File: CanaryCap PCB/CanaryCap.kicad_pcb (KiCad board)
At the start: 2 copper layers, 120 x 30 mm, 59 parts, among them J1 USB_C_Receptacle_USB2.0_16P, J2 Impact Connector, J3 Gas Connector, J4 Battery Connector, Q1 NMOS, Q2 PMOS_Substrate, SW1 SW_MEC_5E, SW2 SW_MEC_5E, SW3 SW_MEC_5E, U1 LMZM23601V5, U2 LM3940 3.3V-SOT223, U3 ESP32-C6FH4, U4 ADXL343

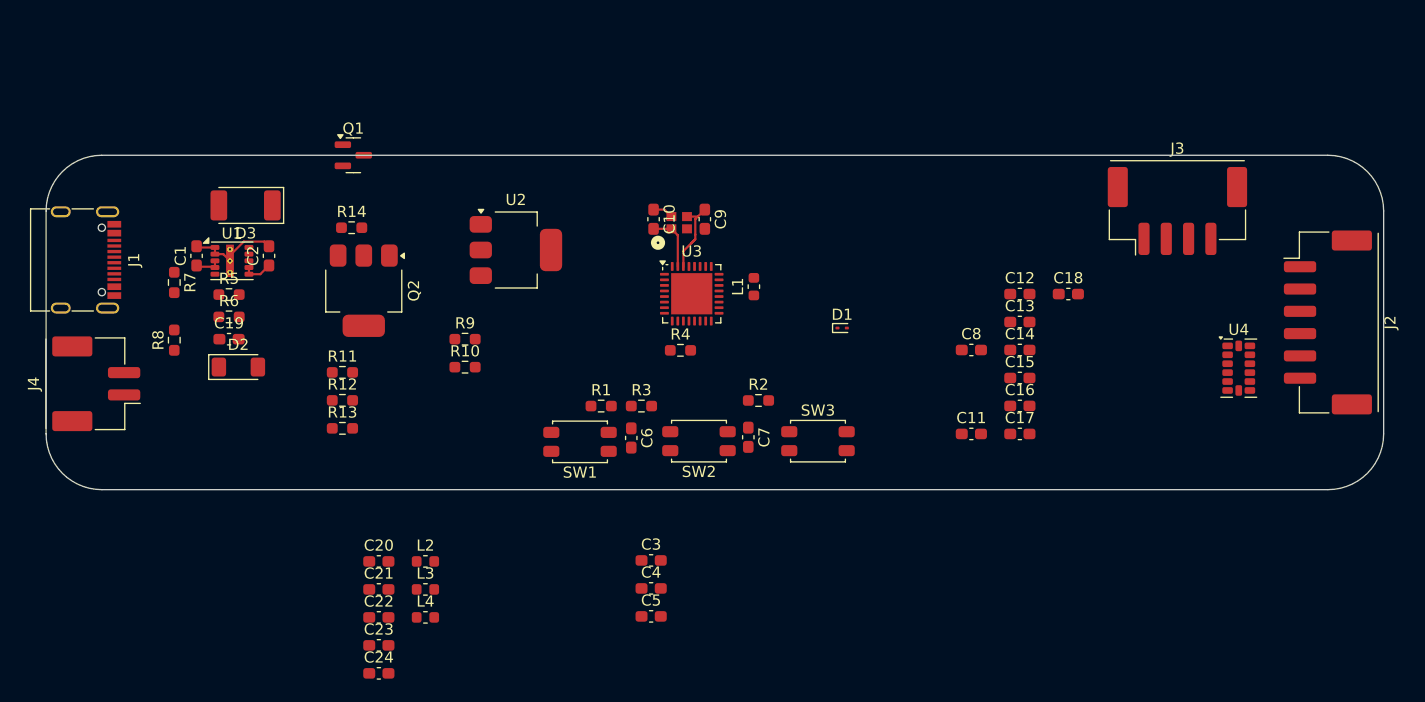
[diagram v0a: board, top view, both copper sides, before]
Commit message: Deleted windows blink
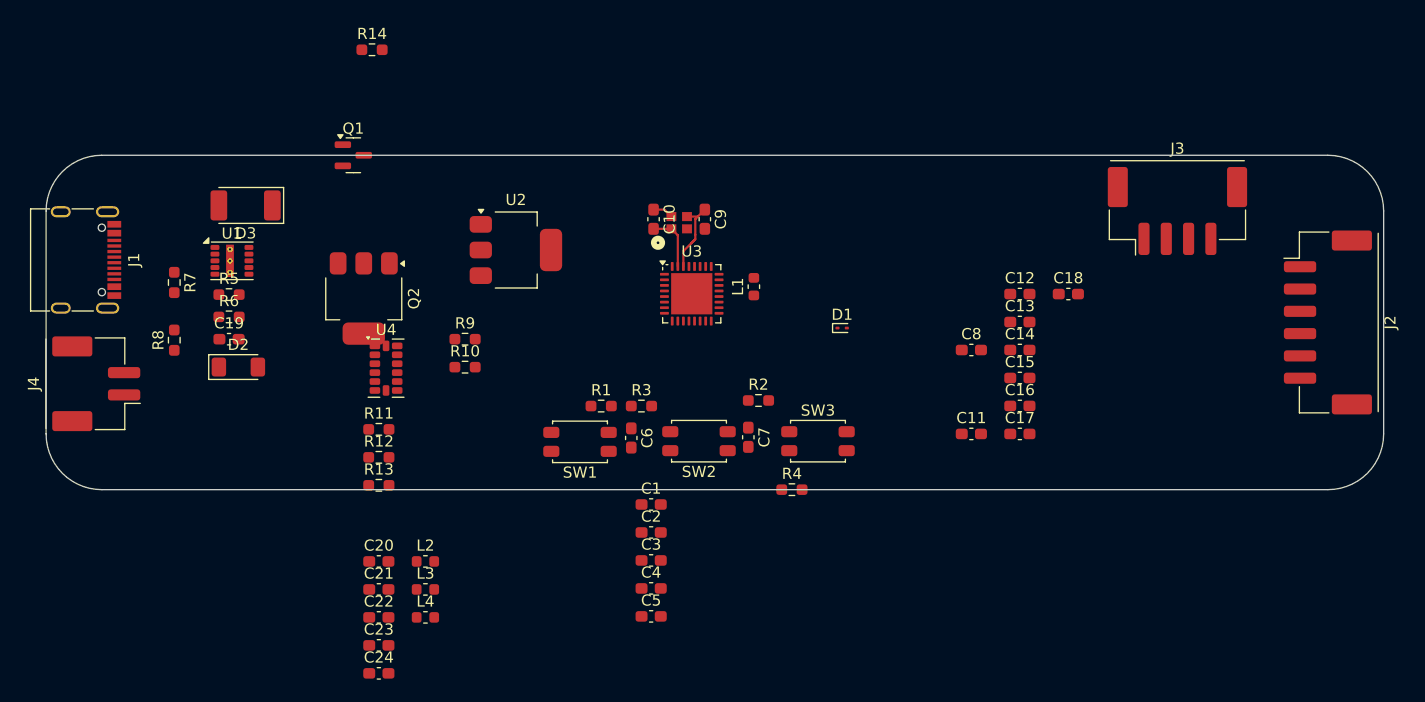
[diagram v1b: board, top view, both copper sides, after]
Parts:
- moved U4 76.5 mm to (131.0, -10.9)
- moved C1 46.5 mm to (154.8, 1.33), turned to 0 degrees
- moved C2 42.3 mm to (154.8, 3.84), turned to 0 degrees
- moved R14 16.1 mm to (129.7, -39.5)
- moved R4 16.0 mm to (167.4, 0.00)
- moved R11 6.06 mm to (130.4, -5.41)
- moved R12 6.06 mm to (130.4, -2.90)
- moved R13 6.06 mm to (130.4, -0.39)
- moved Q2 0.70 mm to (129.0, -17.1)
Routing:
- net GNDREF: track 10.4 -> 1.86 mm
- net +5V_buck: track 2.72 -> 0.00 mm
- net +12V: track 2.28 -> 0.00 mm
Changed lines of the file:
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@@
 	(footprint "Resistor_SMD:R_0603_1608Metric_Pad0.98x0.95mm_HandSolder"
 		(layer "F.Cu")
-		(at 127.0875 -5.5)
+		(at 130.353301 -0.389701)
 		(descr "Resistor SMD 0603 (1608 Metric), square (rectangular) end terminal, IPC-7351 nominal with elongated pad for handsoldering. (Body size source: IPC-SM-782 page 72, https://www.pcb-3d.com/wordpress/wp-content/uploads/ipc-sm-782a_amendment_1_and_2.pdf), generated with kicad-footprint-generator")
 		(tags "resistor handsolder")
@@
 	(footprint "Resistor_SMD:R_0603_1608Metric_Pad0.98x0.95mm_HandSolder"
 		(layer "F.Cu")
-		(at 127.0875 -8.01)
+		(at 130.353301 -2.899701)
 		(descr "Resistor SMD 0603 (1608 Metric), square (rectangular) end terminal, IPC-7351 nominal with elongated pad for handsoldering. (Body size source: IPC-SM-782 page 72, https://www.pcb-3d.com/wordpress/wp-content/uploads/ipc-sm-782a_amendment_1_and_2.pdf), generated with kicad-footprint-generator")
 		(tags "resistor handsolder")
@@
 	(footprint "Resistor_SMD:R_0603_1608Metric_Pad0.98x0.95mm_HandSolder"
 		(layer "F.Cu")
-		(at 127.0875 -10.52)
+		(at 130.353301 -5.409701)
 		(descr "Resistor SMD 0603 (1608 Metric), square (rectangular) end terminal, IPC-7351 nominal with elongated pad for handsoldering. (Body size source: IPC-SM-782 page 72, https://www.pcb-3d.com/wordpress/wp-content/uploads/ipc-sm-782a_amendment_1_and_2.pdf), generated with kicad-footprint-generator")
 		(tags "resistor handsolder")
@@
 	(footprint "Capacitor_SMD:C_0603_1608Metric_Pad1.08x0.95mm_HandSolder"
 		(layer "F.Cu")
-		(at 120.5 -20.975 90)
+		(at 154.783301 3.840299)
 		(descr "Capacitor SMD 0603 (1608 Metric), square (rectangular) end terminal, IPC-7351 nominal with elongated pad for handsoldering. (Body size source: IPC-SM-782 page 76, https://www.pcb-3d.com/wordpress/wp-content/uploads/ipc-sm-782a_amendment_1_and_2.pdf), generated with kicad-footprint-generator")
 		(tags "capacitor handsolder")
 		(property "Reference" "C2"
-			(at 0 -1.43 90)
+			(at 0 -1.43 0)
 			(layer "F.SilkS")
 			(effects
@@
 		)
 		(property "Value" "10uF"
-			(at 0 1.43 90)
+			(at 0 1.43 0)
 			(layer "F.Fab")
 			(effects
@@
 		)
 		(property "Datasheet" "~"
-			(at 0 0 90)
+			(at 0 0 0)
 			(layer "F.Fab")
 			(hide yes)
@@
 		)
 		(property "Description" "Unpolarized capacitor"
-			(at 0 0 90)
+			(at 0 0 0)
 			(layer "F.Fab")
 			(hide yes)
@@
 		)
 		(fp_line
-			(start 1.65 -0.73)
-			(end 1.65 0.73)
+			(start -1.65 -0.73)
+			(end 1.65 -0.73)
 			(stroke
 				(width 0.05)
@@
 		)
 		(fp_line
-			(start -1.65 -0.73)
-			(end 1.65 -0.73)
+			(start -1.65 0.73)
+			(end -1.65 -0.73)
 			(stroke
 				(width 0.05)
@@
 		)
 		(fp_line
-			(start 1.65 0.73)
-			(end -1.65 0.73)
+			(start 1.65 -0.73)
+			(end 1.65 0.73)
 			(stroke
 				(width 0.05)
@@
 		)
 		(fp_line
-			(start -1.65 0.73)
-			(end -1.65 -0.73)
+			(start 1.65 0.73)
+			(end -1.65 0.73)
 			(stroke
 				(width 0.05)
@@
 		)
 		(fp_line
-			(start 0.8 -0.4)
-			(end 0.8 0.4)
+			(start -0.8 -0.4)
+			(end 0.8 -0.4)
 			(stroke
 				(width 0.1)
@@
 		)
 		(fp_line
-			(start -0.8 -0.4)
-			(end 0.8 -0.4)
+			(start -0.8 0.4)
+			(end -0.8 -0.4)
 			(stroke
 				(width 0.1)
@@
 		)
 		(fp_line
-			(start 0.8 0.4)
-			(end -0.8 0.4)
+			(start 0.8 -0.4)
+			(end 0.8 0.4)
 			(stroke
 				(width 0.1)
@@
 		)
 		(fp_line
-			(start -0.8 0.4)
-			(end -0.8 -0.4)
+			(start 0.8 0.4)
+			(end -0.8 0.4)
 			(stroke
 				(width 0.1)
@@
 		)
 		(fp_text user "${REFERENCE}"
-			(at 0 0 90)
+			(at 0 0 0)
 			(layer "F.Fab")
 			(effects
@@
 		)
 		(pad "1" smd roundrect
-			(at -0.8625 0 90)
+			(at -0.8625 0)
 			(size 1.075 0.95)
 			(layers "F.Cu" "F.Mask" "F.Paste")
@@
 		)
 		(pad "2" smd roundrect
-			(at 0.8625 0 90)
+			(at 0.8625 0)
 			(size 1.075 0.95)
 			(layers "F.Cu" "F.Mask" "F.Paste")
@@
 	(footprint "Package_TO_SOT_SMD:SOT-223"
 		(layer "F.Cu")
-		(at 129 -17.85 -90)
+		(at 129 -17.15 -90)
 		(descr "module CMS SOT223 4 pins")
 		(tags "CMS SOT")
@@
 	(footprint "Resistor_SMD:R_0603_1608Metric_Pad0.98x0.95mm_HandSolder"
 		(layer "F.Cu")
-		(at 127.9125 -23.5)
+		(at 129.7425 -39.465)
 		(descr "Resistor SMD 0603 (1608 Metric), square (rectangular) end terminal, IPC-7351 nominal with elongated pad for handsoldering. (Body size source: IPC-SM-782 page 72, https://www.pcb-3d.com/wordpress/wp-content/uploads/ipc-sm-782a_amendment_1_and_2.pdf), generated with kicad-footprint-generator")
 		(tags "resistor handsolder")
@@
 		)
 		(property "Value" "0OHM if needed"
-			(at 0.0875 -1.5 0)
+			(at 0 1.43 0)
 			(layer "F.Fab")
 			(effects
@@
 	(footprint "Resistor_SMD:R_0603_1608Metric_Pad0.98x0.95mm_HandSolder"
 		(layer "F.Cu")
-		(at 157.4125 -12.5)
+		(at 167.4125 0)
 		(descr "Resistor SMD 0603 (1608 Metric), square (rectangular) end terminal, IPC-7351 nominal with elongated pad for handsoldering. (Body size source: IPC-SM-782 page 72, https://www.pcb-3d.com/wordpress/wp-content/uploads/ipc-sm-782a_amendment_1_and_2.pdf), generated with kicad-footprint-generator")
 		(tags "resistor handsolder")
@@
 	(footprint "Package_LGA:LGA-14_3x5mm_P0.8mm_LayoutBorder1x6y"
 		(layer "F.Cu")
-		(at 207.5 -10.9)
+		(at 131 -10.9)
 		(descr "LGA, 14 Pin (http://www.st.com/resource/en/datasheet/lsm303dlhc.pdf), generated with kicad-footprint-generator ipc_noLead_generator.py")
 		(tags "LGA NoLead")
@@
 	(footprint "Capacitor_SMD:C_0603_1608Metric_Pad1.08x0.95mm_HandSolder"
 		(layer "F.Cu")
-		(at 114 -20.975 90)
+		(at 154.783301 1.330299)
 		(descr "Capacitor SMD 0603 (1608 Metric), square (rectangular) end terminal, IPC-7351 nominal with elongated pad for handsoldering. (Body size source: IPC-SM-782 page 76, https://www.pcb-3d.com/wordpress/wp-content/uploads/ipc-sm-782a_amendment_1_and_2.pdf), generated with kicad-footprint-generator")
 		(tags "capacitor handsolder")
 		(property "Reference" "C1"
-			(at 0 -1.43 90)
+			(at 0 -1.43 0)
 			(layer "F.SilkS")
 			(effects
@@
 		)
 		(property "Value" "10uF"
-			(at 0 1.43 90)
+			(at 0 1.43 0)
 			(layer "F.Fab")
 			(effects
@@
 		)
 		(property "Datasheet" "~"
-			(at 0 0 90)
+			(at 0 0 0)
 			(layer "F.Fab")
 			(hide yes)
@@
 		)
 		(property "Description" "Unpolarized capacitor"
-			(at 0 0 90)
+			(at 0 0 0)
 			(layer "F.Fab")
 			(hide yes)
@@
 		)
 		(fp_line
-			(start 1.65 -0.73)
-			(end 1.65 0.73)
+			(start -1.65 -0.73)
+			(end 1.65 -0.73)
 			(stroke
 				(width 0.05)
@@
 		)
 		(fp_line
-			(start -1.65 -0.73)
-			(end 1.65 -0.73)
+			(start -1.65 0.73)
+			(end -1.65 -0.73)
 			(stroke
 				(width 0.05)
@@
 		)
 		(fp_line
-			(start 1.65 0.73)
-			(end -1.65 0.73)
+			(start 1.65 -0.73)
+			(end 1.65 0.73)
 			(stroke
 				(width 0.05)
@@
 		)
 		(fp_line
-			(start -1.65 0.73)
-			(end -1.65 -0.73)
+			(start 1.65 0.73)
+			(end -1.65 0.73)
 			(stroke
 				(width 0.05)
@@
 		)
 		(fp_line
-			(start 0.8 -0.4)
-			(end 0.8 0.4)
+			(start -0.8 -0.4)
+			(end 0.8 -0.4)
 			(stroke
 				(width 0.1)
@@
 		)
 		(fp_line
-			(start -0.8 -0.4)
-			(end 0.8 -0.4)
+			(start -0.8 0.4)
+			(end -0.8 -0.4)
 			(stroke
 				(width 0.1)
@@
 		)
 		(fp_line
-			(start 0.8 0.4)
-			(end -0.8 0.4)
+			(start 0.8 -0.4)
+			(end 0.8 0.4)
 			(stroke
 				(width 0.1)
@@
 		)
 		(fp_line
-			(start -0.8 0.4)
-			(end -0.8 -0.4)
+			(start 0.8 0.4)
+			(end -0.8 0.4)
 			(stroke
 				(width 0.1)
@@
 		)
 		(fp_text user "${REFERENCE}"
-			(at 0 0 90)
+			(at 0 0 0)
 			(layer "F.Fab")
 			(effects
@@
 		)
 		(pad "1" smd roundrect
-			(at -0.8625 0 90)
+			(at -0.8625 0)
 			(size 1.075 0.95)
 			(layers "F.Cu" "F.Mask" "F.Paste")
@@
 		)
 		(pad "2" smd roundrect
-			(at 0.8625 0 90)
+			(at 0.8625 0)
 			(size 1.075 0.95)
 			(layers "F.Cu" "F.Mask" "F.Paste")
@@
 	)
 	(segment
-		(start 115.65 -21.13)
-		(end 115.65 -21.73)
-		(width 0.2)
-		(layer "F.Cu")
-		(net 1)
-	)
-	(segment
-		(start 118.238106 -22.256)
-		(end 120.0815 -22.256)
-		(width 0.2)
-		(layer "F.Cu")
-		(net 1)
-	)
-	(segment
-		(start 120.0815 -22.256)
-		(end 120.5 -21.8375)
-		(width 0.2)
-		(layer "F.Cu")
-		(net 1)
-	)
-	(segment
 		(start 155 -25.125002)
 		(end 155.974996 -25.125002)
@@
 	)
 	(segment
-		(start 117 -21.017894)
-		(end 118.238106 -22.256)
-		(width 0.2)
-		(layer "F.Cu")
-		(net 1)
-	)
-	(segment
-		(start 114 -21.725)
-		(end 115.645 -21.725)
-		(width 0.2)
-		(layer "F.Cu")
-		(net 1)
-	)
-	(segment
-		(start 117 -20.53)
-		(end 117 -21.017894)
-		(width 0.2)
-		(layer "F.Cu")
-		(net 1)
-	)
-	(segment
-		(start 115.645 -21.725)
-		(end 115.65 -21.73)
-		(width 0.2)
-		(layer "F.Cu")
-		(net 1)
-	)
-	(segment
-		(start 116.4 -21.13)
-		(end 117 -20.53)
-		(width 0.2)
-		(layer "F.Cu")
-		(net 1)
-	)
-	(segment
 		(start 155.974996 -25.125002)
 		(end 156.599998 -24.5)
@@
 	)
 	(segment
-		(start 115.65 -21.13)
-		(end 116.4 -21.13)
-		(width 0.2)
-		(layer "F.Cu")
-		(net 1)
-	)
-	(segment
-		(start 115.58 -20)
-		(end 115.65 -19.93)
-		(width 0.2)
-		(layer "F.Cu")
-		(net 2)
-	)
-	(segment
-		(start 115.65 -19.93)
-		(end 115.65 -20.53)
-		(width 0.2)
-		(layer "F.Cu")
-		(net 2)
-	)
-	(segment
-		(start 114 -20)
-		(end 115.58 -20)
-		(width 0.2)
-		(layer "F.Cu")
-		(net 2)
-	)
-	(segment
-		(start 119.7175 -19.33)
-		(end 120.5 -20.1125)
-		(width 0.2)
-		(layer "F.Cu")
-		(net 3)
-	)
-	(segment
-		(start 118.7 -19.33)
-		(end 119.7175 -19.33)
-		(width 0.2)
-		(layer "F.Cu")
-		(net 3)
-	)
-	(segment
-		(start 118.7 -19.33)
-		(end 118.7 -19.93)
-		(width 0.2)
-		(layer "F.Cu")
-		(net 3)
-	)
-	(segment
